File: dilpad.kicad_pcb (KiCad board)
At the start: 2 copper layers, 97.6 x 81.8 mm, 37 parts, among them J1 Conn_01x04_Socket, SW1 RotaryEncoder_Switch, SW2 SW_Push, U1 ProMicro

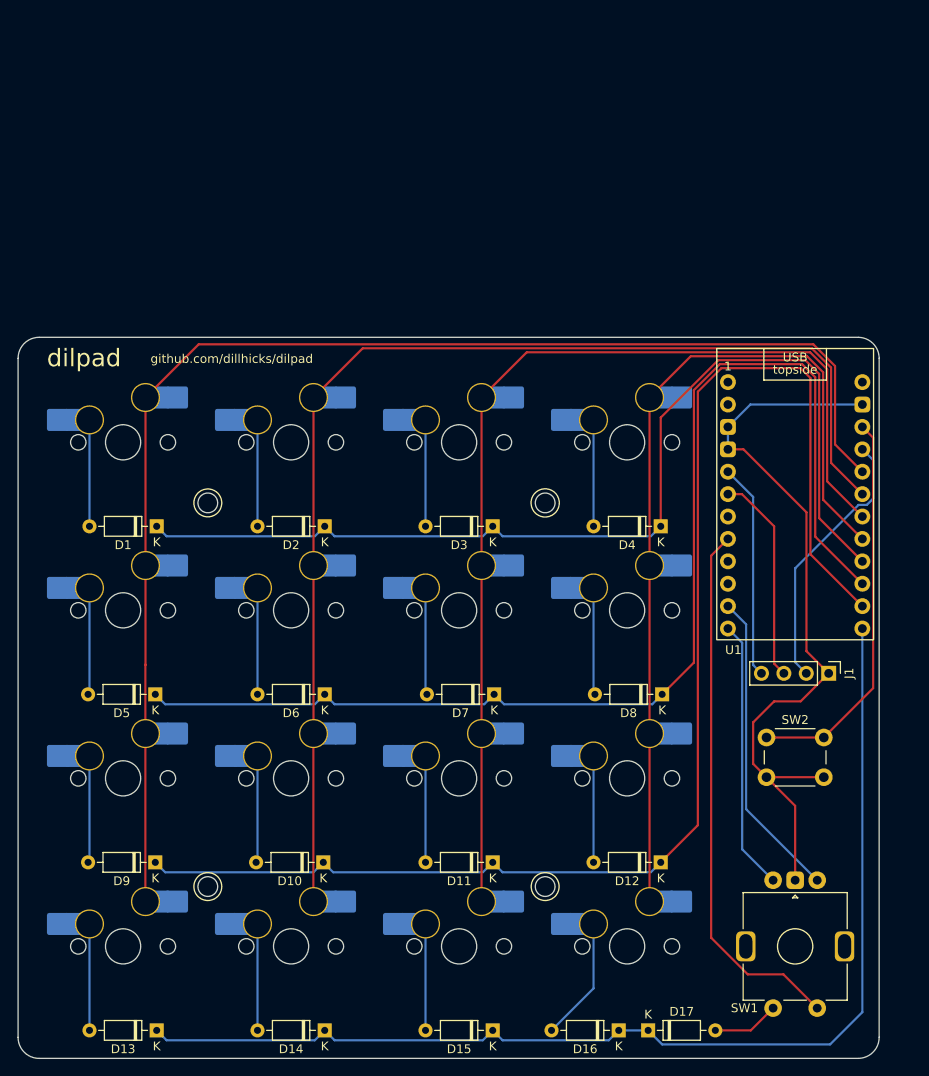
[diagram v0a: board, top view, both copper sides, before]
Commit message: Update Readme, add images, add firmware files
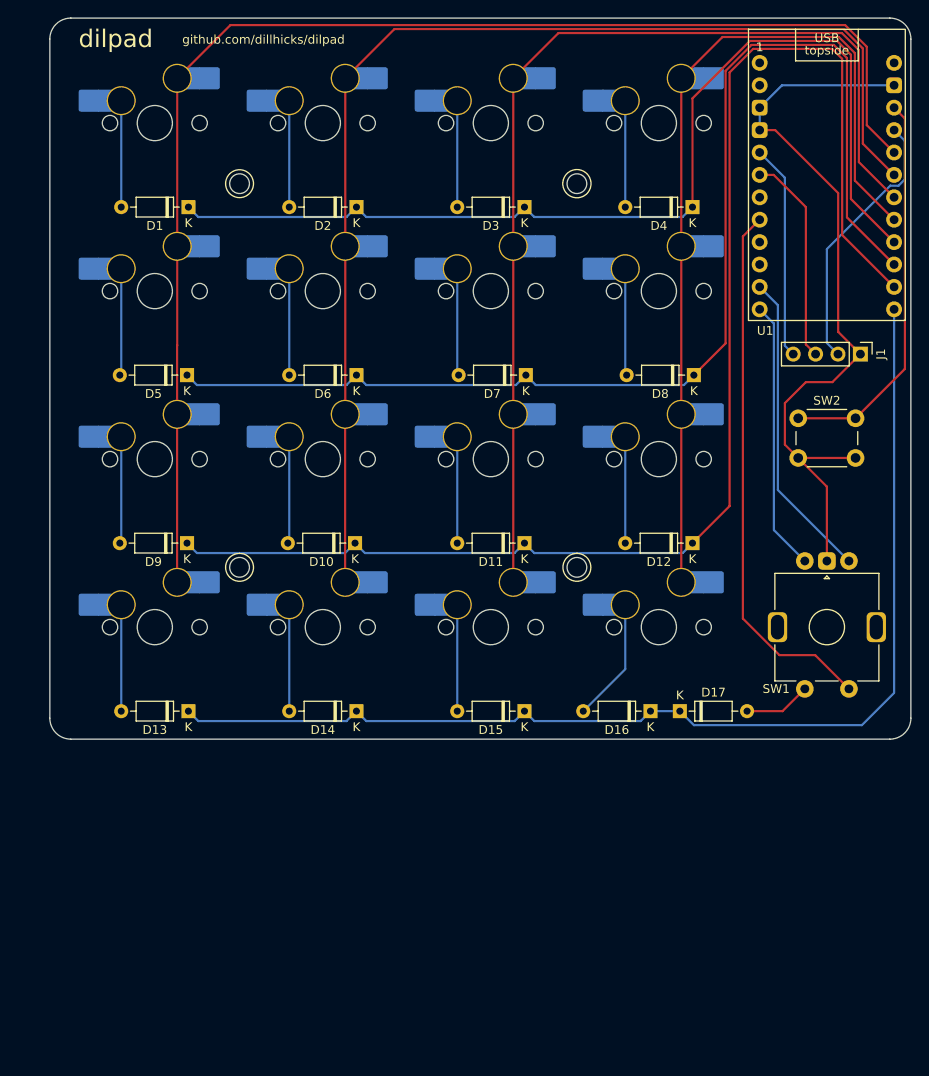
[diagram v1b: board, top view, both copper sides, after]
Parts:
- moved J1 36.4 mm to (186.0, 87.6)
- moved MX5 36.4 mm to (106.0, 80.5)
- moved MX6 36.4 mm to (125.0, 80.5)
- moved MX7 36.4 mm to (144.1, 80.5)
- moved MX8 36.4 mm to (163.1, 80.5)
- moved U1 36.4 mm to (182.2, 68.6)
- moved D1 36.4 mm to (109.8, 71.0)
- moved D10 36.4 mm to (128.7, 109.1)
- moved D11 36.4 mm to (147.9, 109.1)
- moved D12 36.4 mm to (167.0, 109.1)
- moved D13 36.4 mm to (109.8, 128.1)
- moved D14 36.4 mm to (128.9, 128.1)
- moved D15 36.4 mm to (147.9, 128.1)
- moved D16 36.4 mm to (162.2, 128.1)
- moved D17 36.4 mm to (165.5, 128.1)
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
